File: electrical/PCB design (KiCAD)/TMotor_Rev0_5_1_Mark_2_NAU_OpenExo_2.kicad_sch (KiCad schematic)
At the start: 30 parts, among them J2 Conn_01x04_Pin, J3 Conn_01x02_Pin, J4 Conn_01x02_Pin, J5 Conn_01x02_Pin, J6 Conn_01x02_Pin, J7 Conn_01x03_Pin, U5 SN65HVD230DR

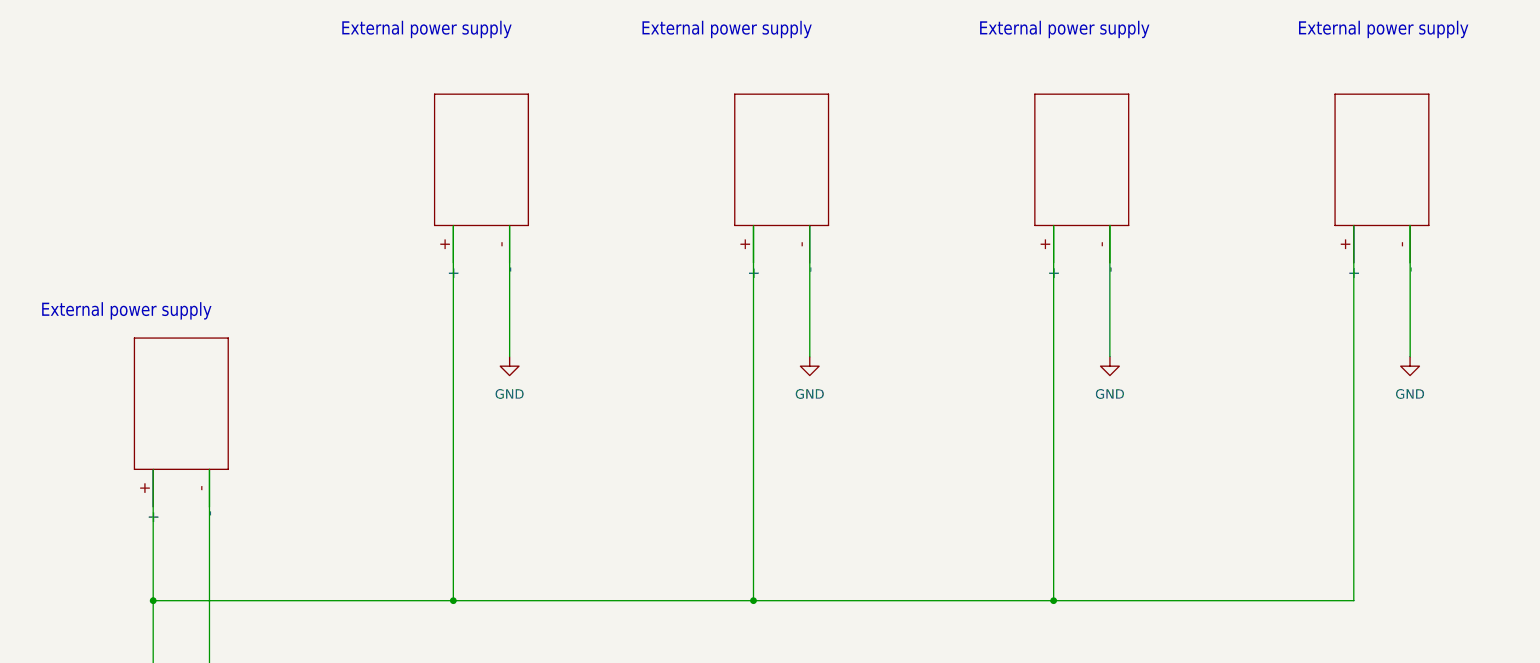
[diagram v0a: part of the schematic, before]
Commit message: Updated KiCAD for next iteration (some minor fixes) ; functional Servo controller and MIT is working over serial
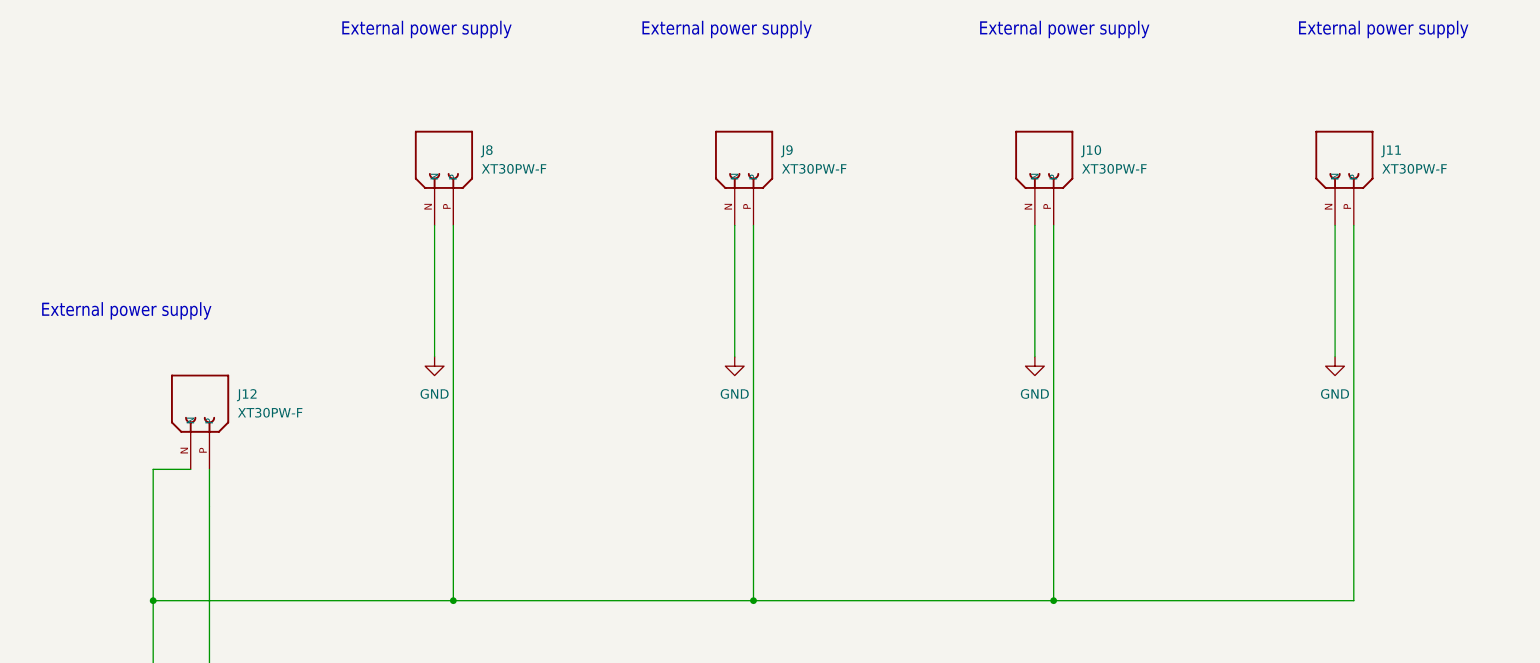
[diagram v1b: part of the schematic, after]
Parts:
- removed XT30UPB-F2, XT30UPB-F4, XT30UPB-F5, XT30UPB-F6, XT30UPB-F7: L_0, TMotor_Rev0_5_1_Mark_2_NAU_OpenExo:XT30UPB-F, symbol TMotor_Rev0_5_1_Mark_2_NAU_OpenExo-eagle-import:XT30UPB-F
- added J10, J11, J12, J8, J9: XT30PW-F, XT30PW-F:AMASS_XT30U-F_1x02_P5.0mm_Vertical, symbol XT30PW-F:XT30PW-F
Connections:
- net GND: now also J10.N, J11.N, J12.P, J8.N, J9.N
- net VBATT: now also J10.P, J11.P, J12.N, J8.P, J9.P
